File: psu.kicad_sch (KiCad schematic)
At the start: 0 parts

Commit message: Add TSP62851x library and LDO on PSU scheme
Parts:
- added C14, C17: 2.2uF, symbol Device:C
- added C15, C16: 470pF, symbol Device:C
- added P1: USB_C_Plug_USB2.0, symbol Connector:USB_C_Plug_USB2.0
- added R2, R3, R4, R5: R, symbol Device:R
- added U2, U3: MIC5205YM5, Package_TO_SOT_SMD:SOT-23-5, symbol Regulator_Linear:MIC5205YM5
- added U4: TPS628511, TSP62851x:SOT-583, symbol TPS62851x:TPS628511
- added U5: TPS628513, TSP62851x:SOT-583, symbol TPS62851x:TPS628513
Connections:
- new net: C16.1, R4.2, R5.1, U3.4 (ADJ)
- new net: C15.1, R2.2, R3.1, U2.4 (ADJ)
- new net +1V3: C17.1, R4.1, U3.5 (OUT)
- new net +2V8: C14.1, R2.1, U2.5 (OUT)
- new net +3V3: U2.1 (IN), U2.3 (EN), U3.1 (IN), U3.3 (EN)
- new net +5V: P1.A4 (VBUS), P1.A9 (VBUS), P1.B4 (VBUS), P1.B9 (VBUS)
- new net GND: C14.2, C15.2, C16.2, C17.2, P1.A1 (GND), P1.A12 (GND), P1.B1 (GND), P1.B12 (GND), P1.S1 (SHIELD), R3.2, R5.2, U2.2 (GND), U3.2 (GND)
- no-connect marks 0 -> 4

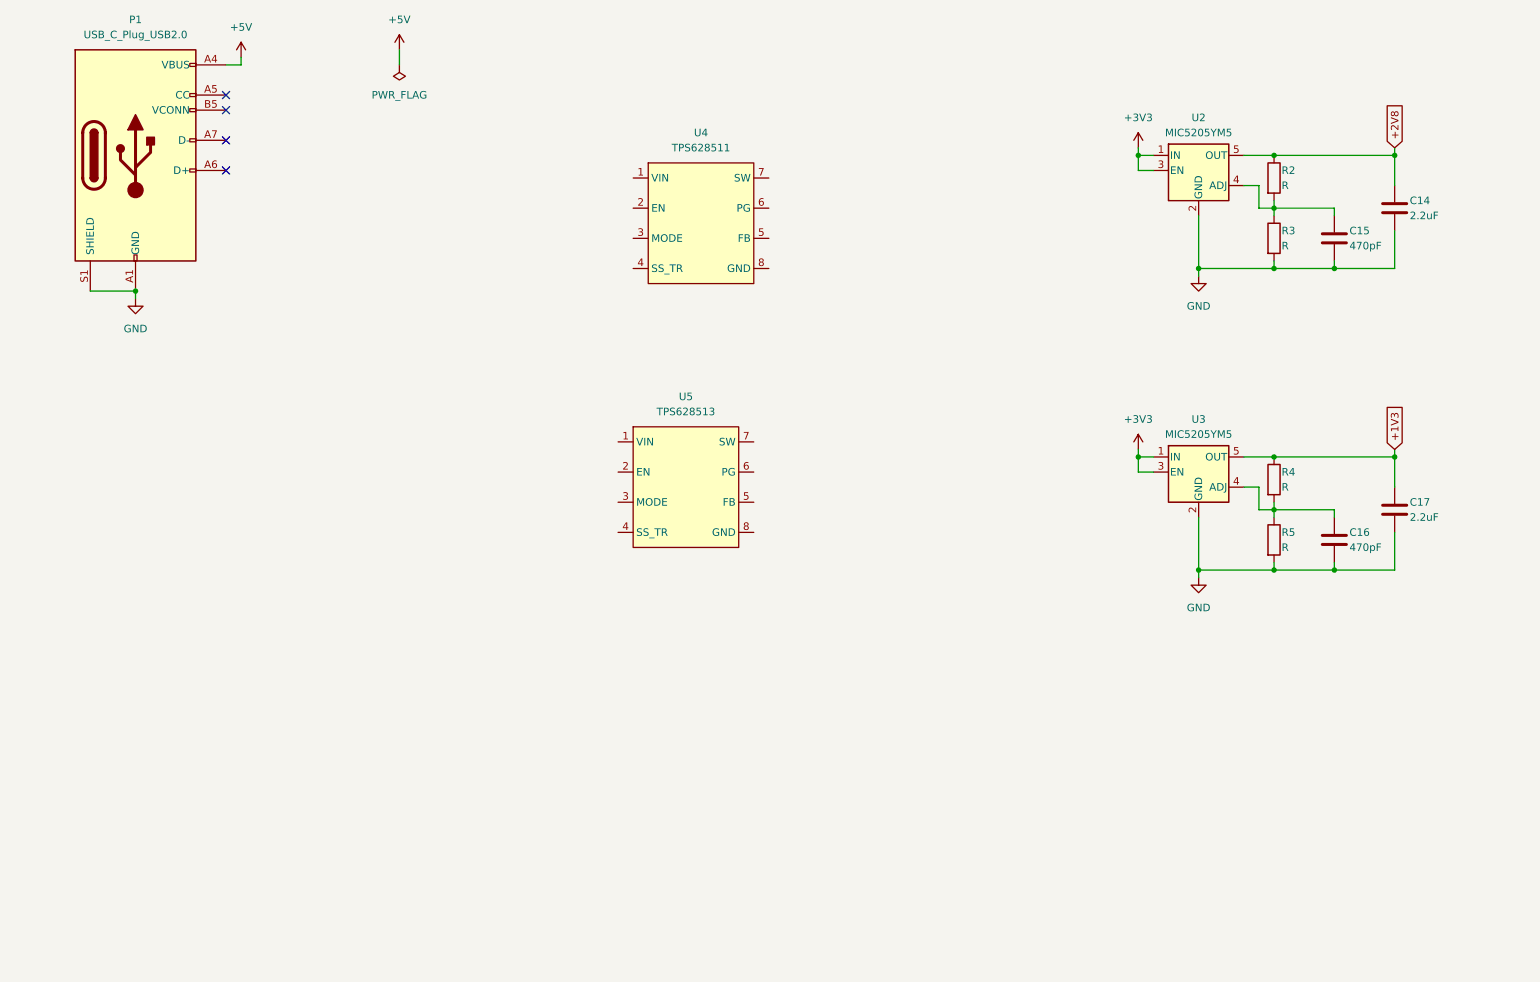
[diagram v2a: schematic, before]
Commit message: Complete schemes, run ERD check tool.
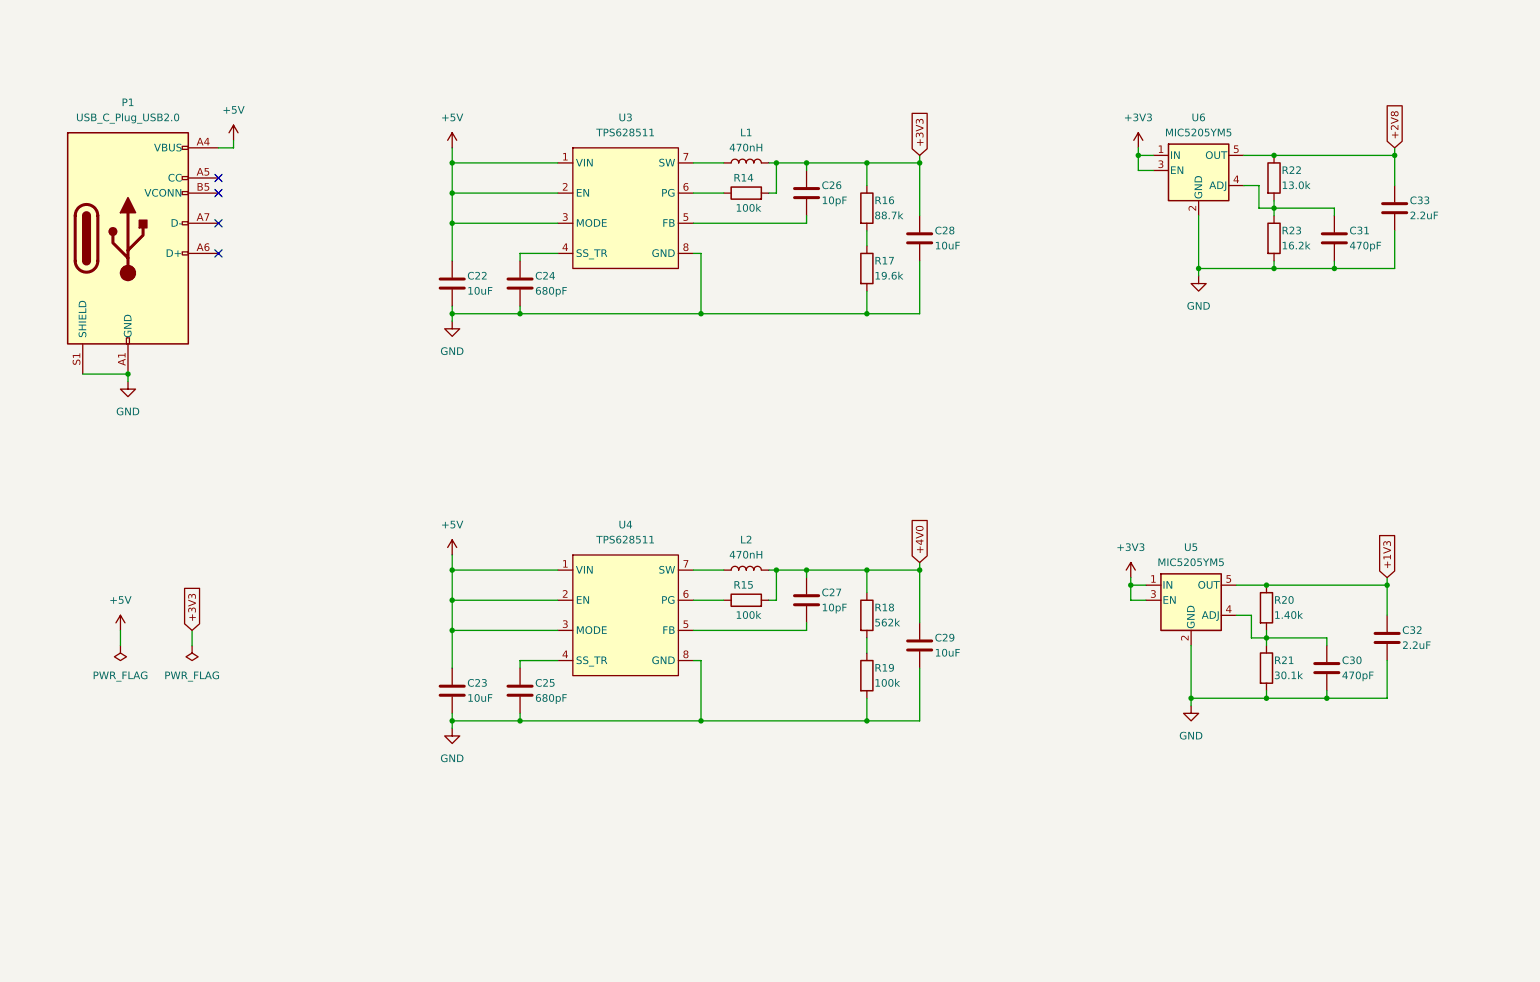
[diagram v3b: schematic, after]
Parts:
- removed U5: TPS628513, TSP62851x:SOT-583, symbol TPS62851x:TPS628513
- added C22, C23, C28, C29: 10uF, symbol Device:C
- added C24, C25: 680pF, symbol Device:C
- added C26, C27: 10pF, symbol Device:C
- added L1, L2: 470nH, symbol Device:L
- added R14, R15, R19: 100k, symbol Device:R
- added R16: 88.7k, symbol Device:R
- added R17: 19.6k, symbol Device:R
- added R18: 562k, symbol Device:R
- added U4: TPS628511, TSP62851x:SOT-583, symbol TPS62851x:TPS628511
- R20: renamed from R4; value R -> 1.40k
- R21: renamed from R5; value R -> 30.1k
- R22: renamed from R2; value R -> 13.0k
- R23: renamed from R3; value R -> 16.2k
- renumbered C16 to C30, C15 to C31, C17 to C32, C14 to C33, U4 to U3, U3 to U5, U2 to U6
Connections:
- net +3V3: now also C26.1, C28.1, L1.2, R14.2, R16.1
- net +5V: now also U3.1 (VIN), U3.2 (EN), U3.3 (MODE), C22.1, C23.1, U4.1 (VIN), U4.2 (EN), U4.3 (MODE)
- net GND: now also U3.8 (GND), C22.2, C23.2, C24.2, C25.2, C28.2, C29.2, R17.2, R19.2, U4.8 (GND)
- net at U3.4 (SS_TR): now also C24.1
- net at U3.5 (FB): now also C26.2
- net at U3.6 (PG): now also R14.1
- net at U3.7 (SW): now also L1.1
- new net: L2.1, U4.7 (SW)
- new net: R16.2, R17.1
- new net: C27.2, U4.5 (FB)
- new net: R15.1, U4.6 (PG)
- new net: C25.1, U4.4 (SS_TR)
- new net: R18.2, R19.1
- new net +4V0: C27.1, C29.1, L2.2, R15.2, R18.1
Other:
- moved on the sheet: C30, C32, P1, R20, R21, U3, U5

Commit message: Assign footprints, change few elements in scheme
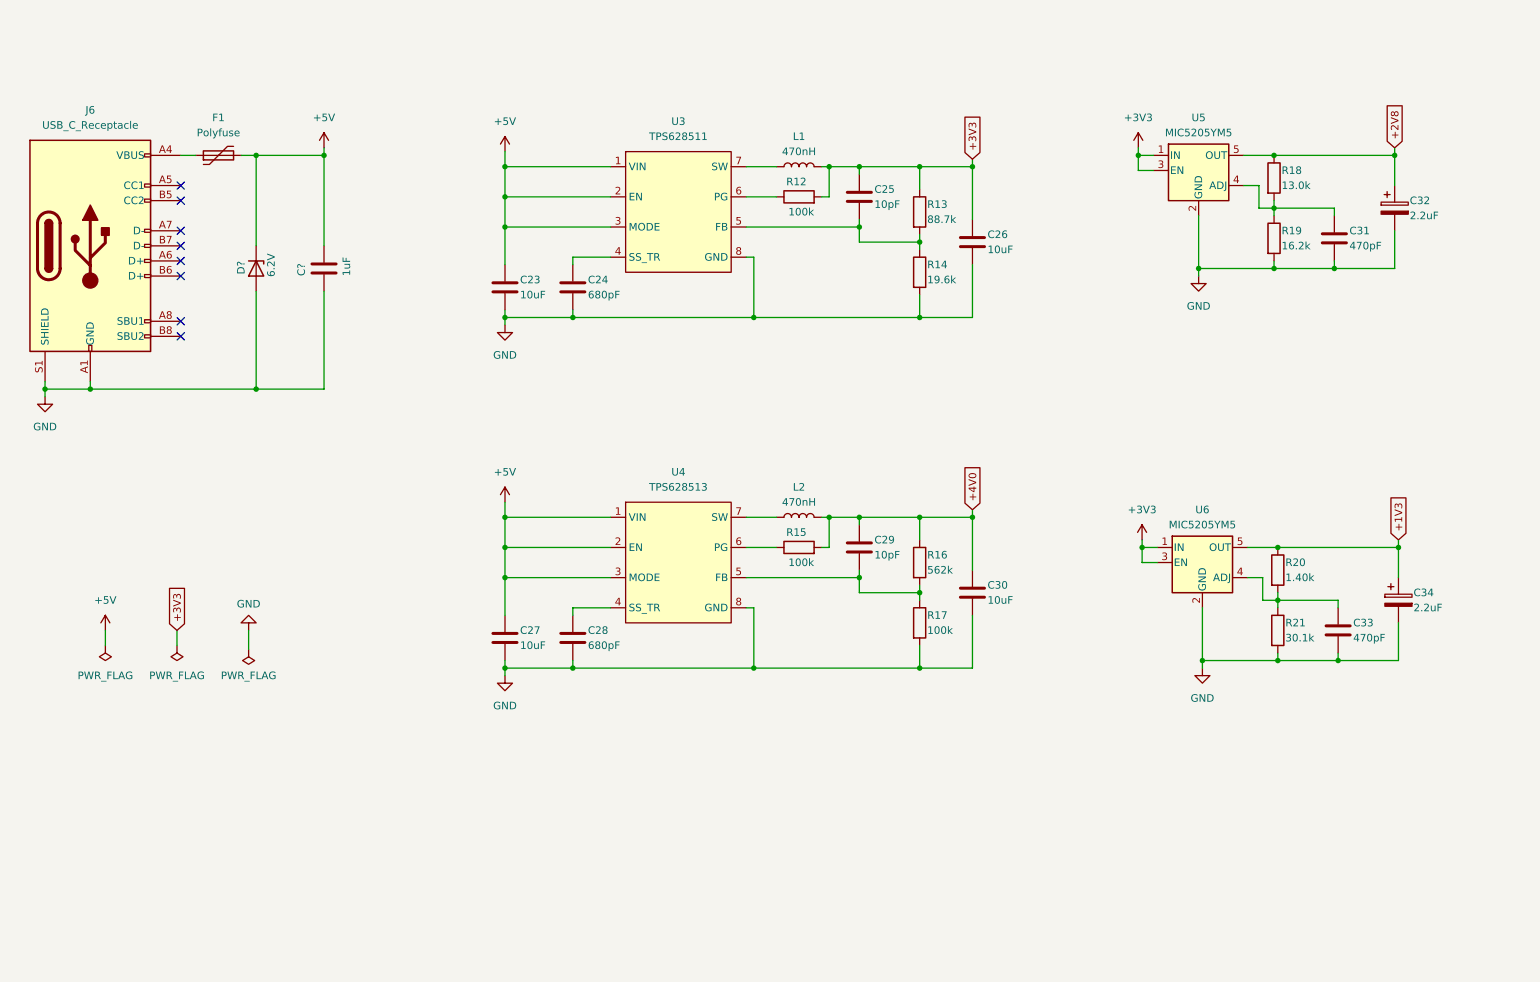
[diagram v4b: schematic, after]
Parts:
- removed C32, C33: 2.2uF, symbol Device:C
- removed P1: USB_C_Plug_USB2.0, symbol Connector:USB_C_Plug_USB2.0
- removed U3, U4: TPS628511, TSP62851x:SOT-583, symbol TPS62851x:TPS628511
- added C32, C34: 2.2uF, Capacitor_SMD:C_0603_1608Metric_Pad1.08x0.95mm_HandSolder, symbol Device:C_Polarized
- added C?: 1uF, Capacitor_SMD:C_0603_1608Metric_Pad1.08x0.95mm_HandSolder, symbol Device:C
- added D?: 6.2V, Diode_SMD:D_SOD-323_HandSoldering, symbol Device:D_Zener
- added F1: Polyfuse, Fuse:Fuse_1812_4532Metric_Pad1.30x3.40mm_HandSolder, symbol Device:Polyfuse
- added J6: USB_C_Receptacle, Connector_USB:USB_C_Receptacle_JAE_DX07S016JA1R1500, symbol Connector:USB_C_Receptacle_USB2.0
- added U3: TPS628511, TSP62851x:SOT-583, symbol TPS62851x:TPS62851x
- added U4: TPS628513, TSP62851x:SOT-583, symbol TPS62851x:TPS62851x
- C23: renamed from C22; footprint (none) -> Capacitor_SMD:C_0603_1608Metric_Pad1.08x0.95mm_HandSolder
- C24, C31: footprint (none) -> Capacitor_SMD:C_0603_1608Metric_Pad1.08x0.95mm_HandSolder
- C25: renamed from C26; footprint (none) -> Capacitor_SMD:C_0603_1608Metric_Pad1.08x0.95mm_HandSolder
- C26: renamed from C28; footprint (none) -> Capacitor_SMD:C_0603_1608Metric_Pad1.08x0.95mm_HandSolder
- C27: renamed from C23; footprint (none) -> Capacitor_SMD:C_0603_1608Metric_Pad1.08x0.95mm_HandSolder
- C28: renamed from C25; footprint (none) -> Capacitor_SMD:C_0603_1608Metric_Pad1.08x0.95mm_HandSolder
- C29: renamed from C27; footprint (none) -> Capacitor_SMD:C_0603_1608Metric_Pad1.08x0.95mm_HandSolder
- C30: renamed from C29; footprint (none) -> Capacitor_SMD:C_0603_1608Metric_Pad1.08x0.95mm_HandSolder
- C33: renamed from C30; footprint (none) -> Capacitor_SMD:C_0603_1608Metric_Pad1.08x0.95mm_HandSolder
- L1, L2: footprint (none) -> Inductor_SMD:L_Vishay_IHLP-1616
- R12: renamed from R14; footprint (none) -> Resistor_SMD:R_0603_1608Metric_Pad0.98x0.95mm_HandSolder
- R13: renamed from R16; footprint (none) -> Resistor_SMD:R_0603_1608Metric_Pad0.98x0.95mm_HandSolder
- R14: renamed from R17; footprint (none) -> Resistor_SMD:R_0603_1608Metric_Pad0.98x0.95mm_HandSolder
- R15, R20, R21: footprint (none) -> Resistor_SMD:R_0603_1608Metric_Pad0.98x0.95mm_HandSolder
- R16: renamed from R18; footprint (none) -> Resistor_SMD:R_0603_1608Metric_Pad0.98x0.95mm_HandSolder
- R17: renamed from R19; footprint (none) -> Resistor_SMD:R_0603_1608Metric_Pad0.98x0.95mm_HandSolder
- R18: renamed from R22; footprint (none) -> Resistor_SMD:R_0603_1608Metric_Pad0.98x0.95mm_HandSolder
- R19: renamed from R23; footprint (none) -> Resistor_SMD:R_0603_1608Metric_Pad0.98x0.95mm_HandSolder
- renumbered U6 to U5, U5 to U6
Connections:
- net +1V3: now also C34.1
- net +2V8: now also C32.1
- net +5V: now also C?.1, D?.1 (K), F1.2, U3.1 (VIN), U3.2 (EN), U3.3 (MODE), U4.1 (VIN), U4.2 (EN), U4.3 (MODE)
- net GND: now also C32.2, C34.2, C?.2, D?.2 (A), J6.A1 (GND), J6.A12 (GND), J6.B1 (GND), J6.B12 (GND), J6.S1 (SHIELD), U3.8 (GND), U4.8 (GND)
- net at R12.1: now also U3.6 (PG)
- net at L2.1: now also U4.7 (SW)
- net at R13.2, R14.1: now also C25.2, U3.5 (FB)
- net at C29.2: now also R16.2, R17.1, U4.5 (FB)
- net at R15.1: now also U4.6 (PG)
- net at C24.1: now also U3.4 (SS_TR)
- net at C28.1: now also U4.4 (SS_TR)
- net at L1.1: now also U3.7 (SW)
- new net: F1.1, J6.A4 (VBUS), J6.A9 (VBUS), J6.B4 (VBUS), J6.B9 (VBUS)
- no-connect marks 4 -> 8
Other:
- moved on the sheet: C23, C24, C25, C26, C27, C28, C29, C30, C33, L1, L2, R12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

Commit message: Create bill of materials
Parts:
- C32, C34: value 2.2uF -> 2.2uF_tantalum
- F1: value Polyfuse -> Polyfuse_3A
- J6: value USB_C_Receptacle -> USB_C_receptacle
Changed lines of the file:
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@@
       (effects (font (size 1.27 1.27)) (justify left))
     )
-    (property "Value" "2.2uF" (at 257.175 129.54 0)
+    (property "Value" "2.2uF_tantalum" (at 257.175 129.54 0)
       (effects (font (size 1.27 1.27)) (justify left))
     )
@@
       (effects (font (size 1.27 1.27)))
     )
-    (property "Value" "USB_C_Receptacle" (at 34.29 48.26 0)
+    (property "Value" "USB_C_receptacle" (at 34.29 48.26 0)
       (effects (font (size 1.27 1.27)))
     )
@@
       (effects (font (size 1.27 1.27)) hide)
     )
-    (property "Datasheet" "https://www.usb.org/sites/default/files/documents/usb_type-c.zip" (at 38.1 68.58 0)
+    (property "Datasheet" "~" (at 38.1 68.58 0)
       (effects (font (size 1.27 1.27)) hide)
     )
@@
       (effects (font (size 1.27 1.27)))
     )
-    (property "Value" "Polyfuse" (at 55.88 49.53 90)
+    (property "Value" "Polyfuse_3A" (at 55.88 49.53 90)
       (effects (font (size 1.27 1.27)))
     )
@@
       (effects (font (size 1.27 1.27)) (justify left))
     )
-    (property "Value" "2.2uF" (at 256.54 63.5 0)
+    (property "Value" "2.2uF_tantalum" (at 256.54 63.5 0)
       (effects (font (size 1.27 1.27)) (justify left))
     )
